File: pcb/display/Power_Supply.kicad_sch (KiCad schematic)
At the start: 59 parts, among them U10 TPS259474x, U11 LV3842, U6 AP2210, U9 SIC438BED-T1-GE3

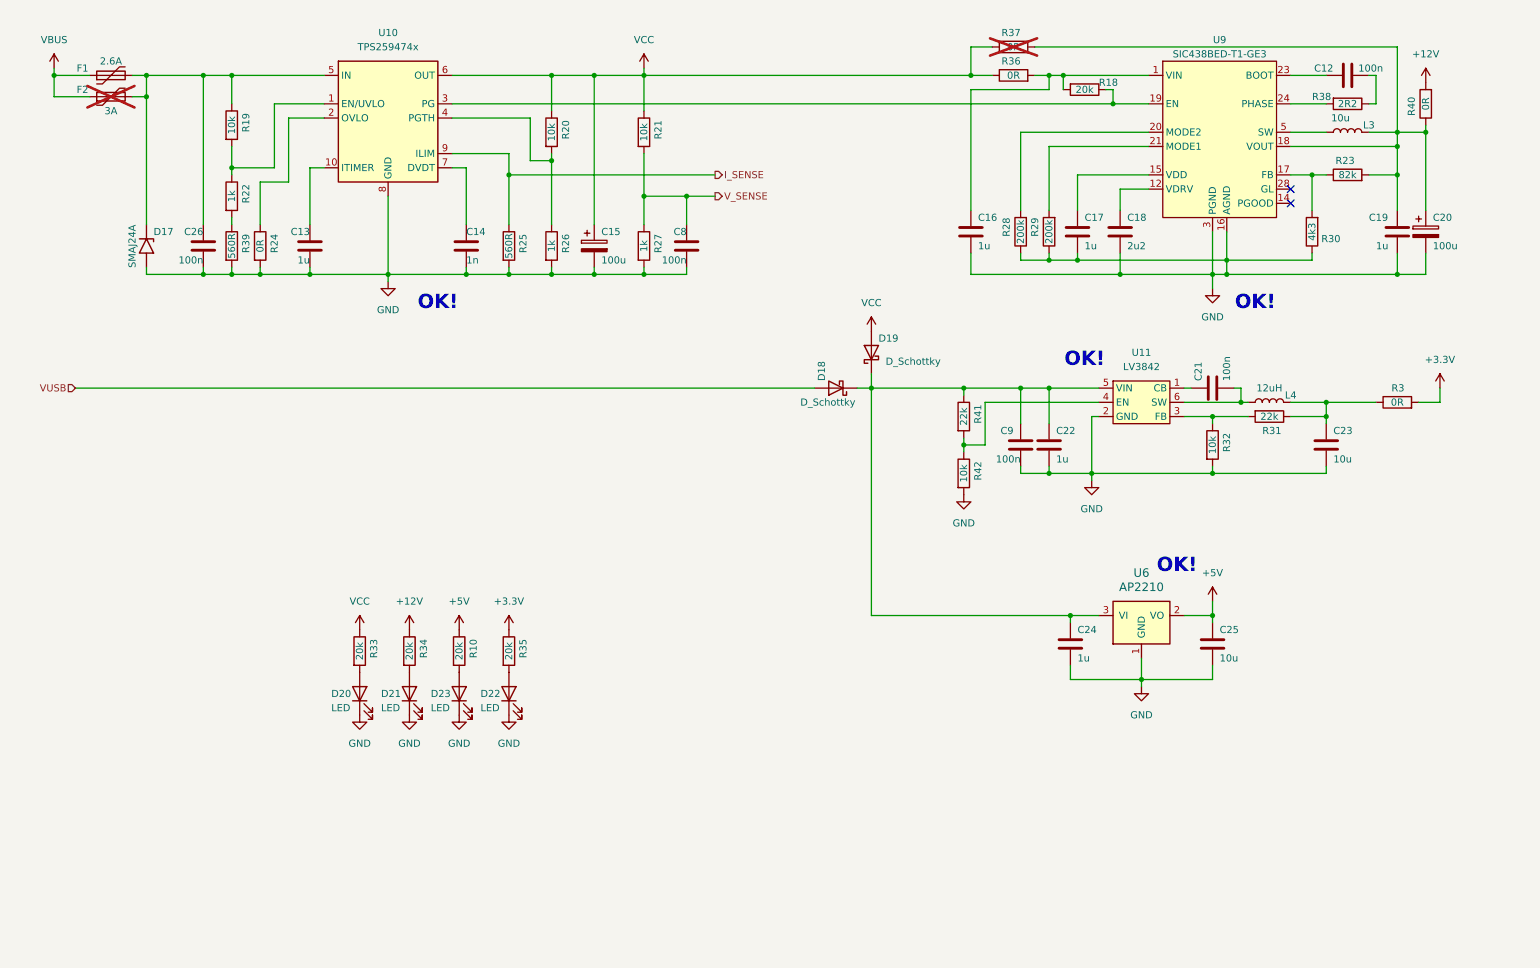
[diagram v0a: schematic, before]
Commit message: Final Version of Prototype Rev. 00
Switched back to PCA9685 for PWM, removed high side switch
Updated some component values
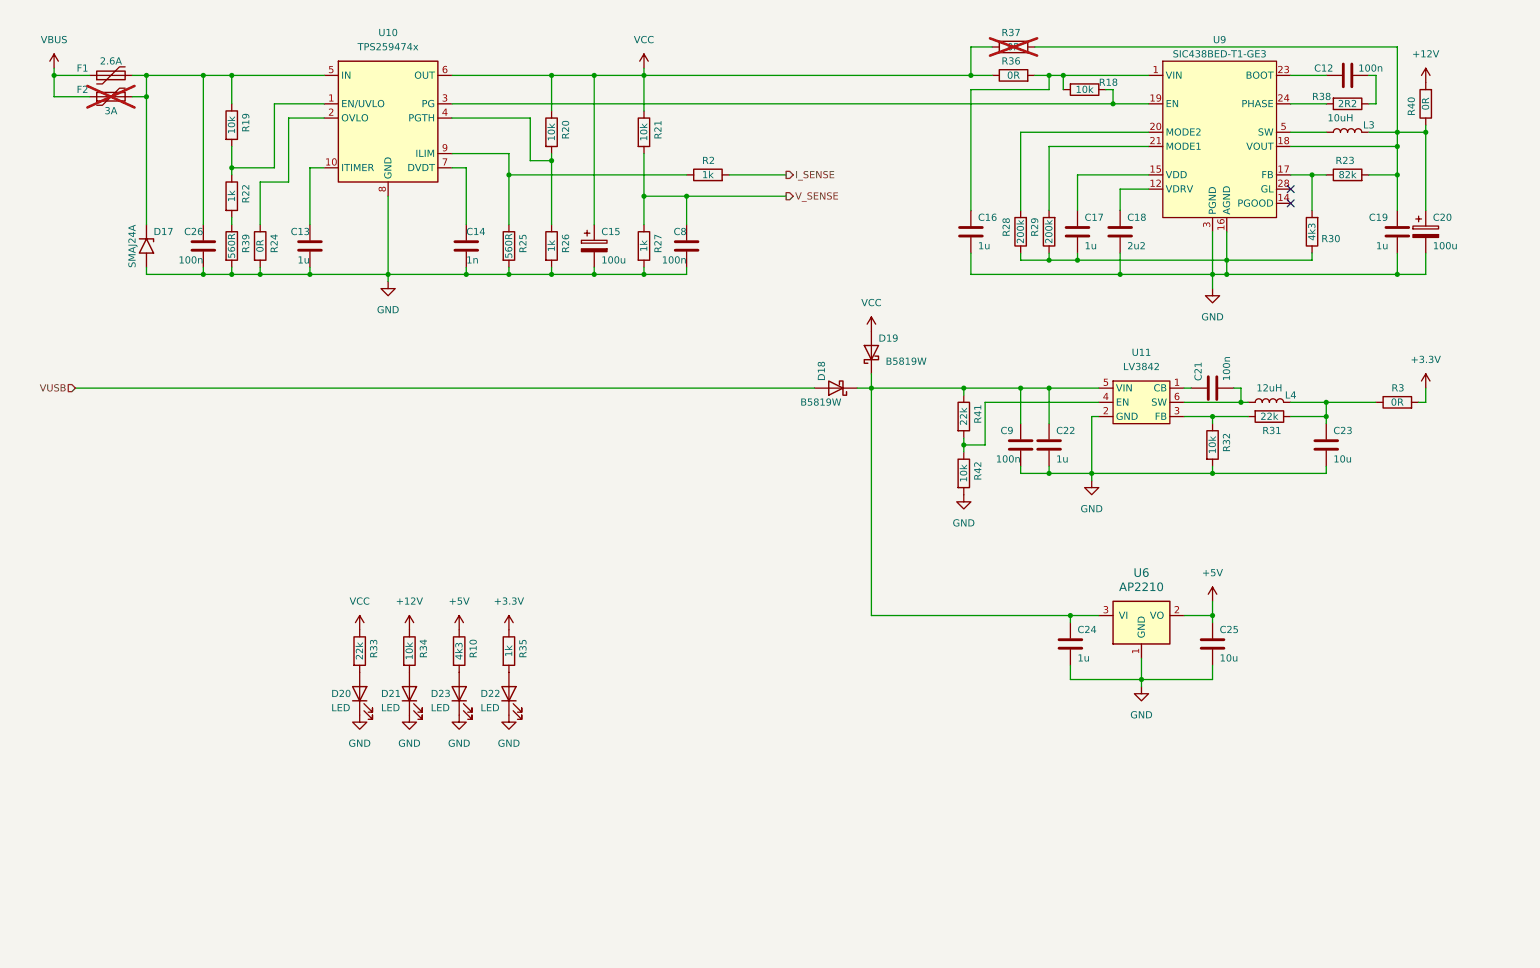
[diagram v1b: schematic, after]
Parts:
- added R2: 1k, Resistor_SMD:R_0603_1608Metric, symbol Device:R
- D18, D19: value D_Schottky -> B5819W
- L3: value 10u -> 10uH
- R10: value 20k -> 4k3
- R18, R34: value 20k -> 10k
- R33: value 20k -> 22k
- R35: value 20k -> 1k
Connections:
- net I_SENSE: now also R2.2; no longer R25.1, U10.9 (ILIM)
- new net: R2.1, R25.1, U10.9 (ILIM)
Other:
- note removed: "OK!"
- title: (none) -> Power Supply
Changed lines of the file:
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@@
 	(paper "A4")
 	(title_block
-		(date "2024-11-11")
+		(title "Power Supply")
+		(date "2024-11-17")
 		(rev "00")
 		(company "Ravenspark")
@@
 	(wire
 		(pts
+			(xy 142.24 43.18) (xy 152.4 43.18)
+		)
+		(stroke
+			(width 0)
+			(type default)
+		)
+	)
+	(wire
+		(pts
 			(xy 201.93 27.94) (xy 201.93 25.4)
 		)
@@
 	(wire
 		(pts
-			(xy 265.43 83.82) (xy 269.24 83.82)
+			(xy 265.43 83.82) (xy 266.7 83.82)
 		)
 		(stroke
@@
 	(wire
 		(pts
-			(xy 269.24 81.28) (xy 269.24 83.82)
+			(xy 266.7 81.28) (xy 266.7 83.82)
 		)
 		(stroke
@@
 	(wire
 		(pts
-			(xy 102.87 43.18) (xy 139.7 43.18)
+			(xy 102.87 43.18) (xy 134.62 43.18)
 		)
 		(stroke
@@
 	(wire
 		(pts
-			(xy 134.62 46.99) (xy 139.7 46.99)
+			(xy 134.62 46.99) (xy 152.4 46.99)
 		)
 		(stroke
@@
 		)
 	)
-	(text "OK!"
-		(exclude_from_sim no)
-		(at 222.25 113.03 0)
-		(effects
-			(font
-				(size 2.54 2.54)
-				(thickness 0.254)
-				(bold yes)
-				(color 255 176 0 1)
-			)
-		)
-	)
-	(text "OK!"
-		(exclude_from_sim no)
-		(at 205.74 76.2 0)
-		(effects
-			(font
-				(size 2.54 2.54)
-				(thickness 0.254)
-				(bold yes)
-				(color 255 176 0 1)
-			)
-		)
-	)
-	(text "OK!"
-		(exclude_from_sim no)
-		(at 90.17 66.04 0)
-		(effects
-			(font
-				(size 2.54 2.54)
-				(thickness 0.254)
-				(bold yes)
-				(color 255 176 0 1)
-			)
-		)
-	)
-	(text "OK!"
-		(exclude_from_sim no)
-		(at 236.22 66.04 0)
-		(effects
-			(font
-				(size 2.54 2.54)
-				(thickness 0.254)
-				(bold yes)
-				(color 255 176 0 1)
-			)
-		)
-	)
 	(hierarchical_label "VUSB"
 		(shape input)
@@
 	(hierarchical_label "I_SENSE"
 		(shape output)
-		(at 139.7 43.18 0)
+		(at 152.4 43.18 0)
 		(fields_autoplaced yes)
 		(effects
@@
 	(hierarchical_label "V_SENSE"
 		(shape output)
-		(at 139.7 46.99 0)
+		(at 152.4 46.99 0)
 		(fields_autoplaced yes)
 		(effects
@@
 			)
 		)
-		(property "Value" "D_Schottky"
+		(property "Value" "B5819W"
 			(at 170.18 76.5174 90)
 			(effects
@@
 	(symbol
 		(lib_id "power:+3.3V")
-		(at 269.24 81.28 0)
+		(at 266.7 81.28 0)
 		(unit 1)
 		(exclude_from_sim no)
@@
 		(fields_autoplaced yes)
 		(property "Reference" "#PWR067"
-			(at 269.24 85.09 0)
+			(at 266.7 85.09 0)
 			(effects
 				(font
@@
 		)
 		(property "Value" "+3.3V"
-			(at 269.24 76.2 0)
+			(at 266.7 76.2 0)
 			(effects
 				(font
@@
 		)
 		(property "Footprint" ""
-			(at 269.24 81.28 0)
+			(at 266.7 81.28 0)
 			(effects
 				(font
@@
 		)
 		(property "Datasheet" ""
-			(at 269.24 81.28 0)
+			(at 266.7 81.28 0)
 			(effects
 				(font
@@
 		)
 		(property "Description" "Power symbol creates a global label with name \"+3.3V\""
-			(at 269.24 81.28 0)
+			(at 266.7 81.28 0)
 			(effects
 				(font
@@
 			)
 		)
-		(property "Value" "20k"
+		(property "Value" "10k"
 			(at 205.74 27.94 90)
 			(effects
@@
 			)
 		)
-		(property "Value" "D_Schottky"
+		(property "Value" "B5819W"
 			(at 154.94 83.82 0)
 			(effects
@@
 			)
 		)
-		(property "Value" "20k"
+		(property "Value" "1k"
 			(at 102.87 128.27 90)
 			(effects
@@
 	)
 	(symbol
+		(lib_id "Device:R")
+		(at 138.43 43.18 90)
+		(unit 1)
+		(exclude_from_sim no)
+		(in_bom yes)
+		(on_board yes)
+		(dnp no)
+		(property "Reference" "R2"
+			(at 139.7 40.64 90)
+			(effects
+				(font
+					(size 1.27 1.27)
+				)
+				(justify left)
+			)
+		)
+		(property "Value" "1k"
+			(at 138.43 43.18 90)
+			(effects
+				(font
+					(size 1.27 1.27)
+				)
+			)
+		)
+		(property "Footprint" "Resistor_SMD:R_0603_1608Metric"
+			(at 138.43 44.958 90)
+			(effects
+				(font
+					(size 1.27 1.27)
+				)
+				(hide yes)
+			)
+		)
+		(property "Datasheet" "~"
+			(at 138.43 43.18 0)
+			(effects
+				(font
+					(size 1.27 1.27)
+				)
+				(hide yes)
+			)
+		)
+		(property "Description" "Resistor"
+			(at 138.43 43.18 0)
+			(effects
+				(font
+					(size 1.27 1.27)
+				)
+				(hide yes)
+			)
+		)
+		(pin "1"
+		)
+		(pin "2"
+		)
+		(instances
+			(project "Display"
+				(path "/909ae33d-387b-4690-b0aa-ba1ded8f44db/89a87f9d-0057-4f99-b34f-09ac7f75c0d0"
+					(reference "R2")
+					(unit 1)
+				)
+			)
+		)
+	)
+	(symbol
 		(lib_id "power:GND")
 		(at 93.98 139.7 0)
@@
 			)
 		)
-		(property "Value" "20k"
+		(property "Value" "10k"
 			(at 85.09 128.27 90)
 			(effects
@@
 			)
 		)
-		(property "Value" "20k"
+		(property "Value" "4k3"
 			(at 93.98 128.27 90)
 			(effects
@@
 			)
 		)
-		(property "Value" "10u"
+		(property "Value" "10uH"
 			(at 251.46 33.02 90)
 			(effects
@@
 			)
 		)
-		(property "Value" "20k"
+		(property "Value" "22k"
 			(at 76.2 128.27 90)
 			(effects

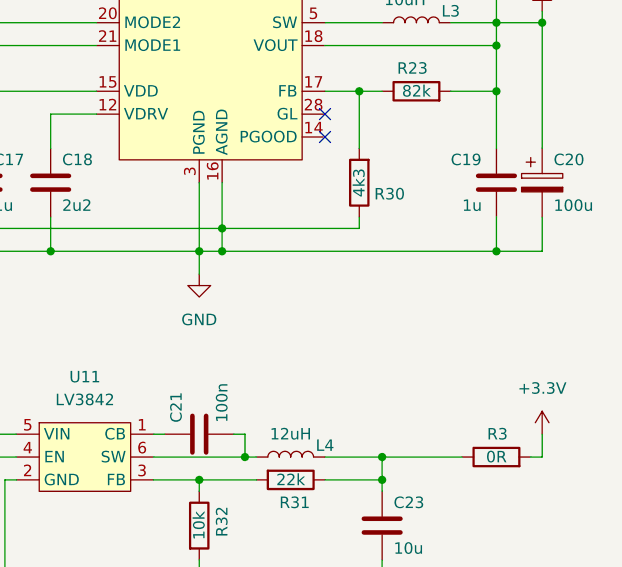
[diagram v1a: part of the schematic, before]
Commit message: Marked known issues in schematic
Add gitignore
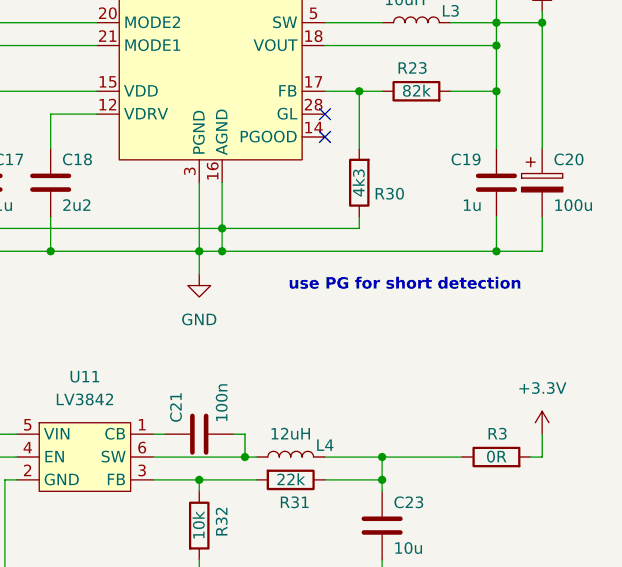
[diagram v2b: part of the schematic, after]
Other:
- note added: "use PG for short detection"
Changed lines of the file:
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@@
+		)
+	)
+	(text "use PG for short detection"
+		(exclude_from_sim no)
+		(at 251.46 64.77 0)
+		(effects
+			(font
+				(size 1.27 1.27)
+				(thickness 0.254)
+				(bold yes)
+				(color 255 153 0 1)
+			)
 		)
 	)
